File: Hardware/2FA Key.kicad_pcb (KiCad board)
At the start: 2 copper layers, 35.2 x 18.5 mm, 22 parts, among them J1 USB_A_PCB_Edge_receptacle, SW1 Push Button, U1 USBLC6-2SC6, U2 ATECC608B-SSHDA, U3 AP2112K‑3.3, U4 STM32L432KCU6

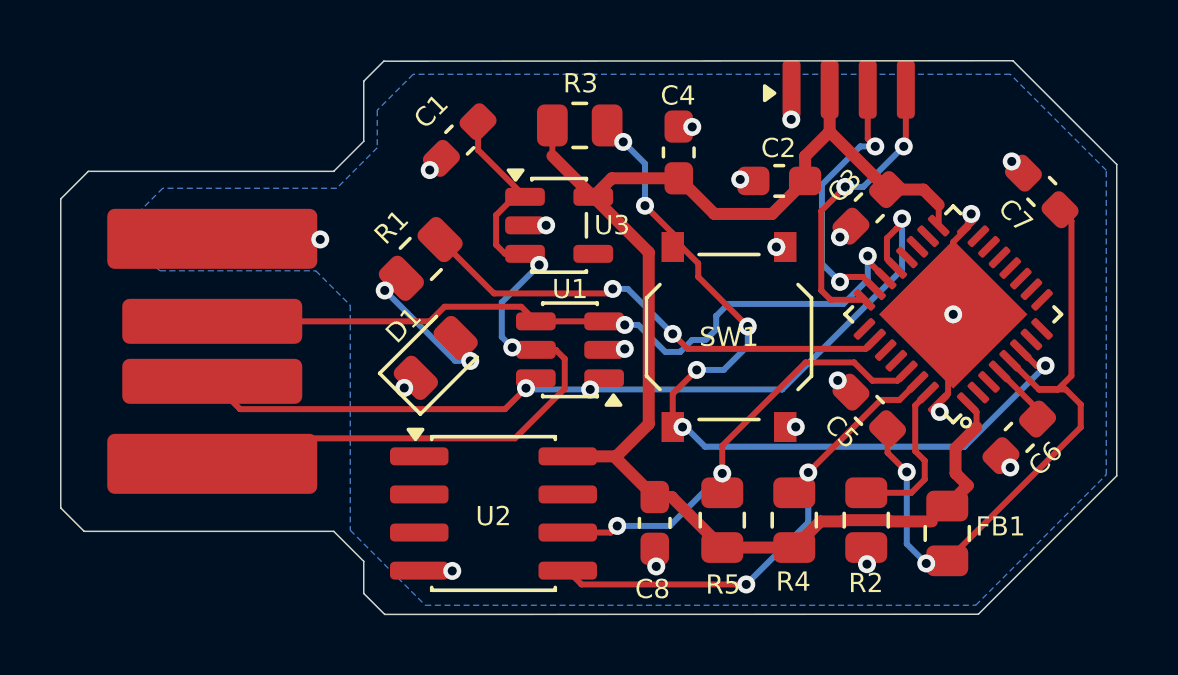
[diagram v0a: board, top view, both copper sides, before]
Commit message: Reorganize repo and rewrite README; add Ed25519 and compliance/programmable content
Move SSH guide to Guides/ and FIDO/RoHS docs to Compliance/; add Programmable/ (HID Injection, Mouse Jiggler, hardware, case), 3D Printable/, BOM datasheets, renders. Rewrite README around 2FAK V1C and Programmable 2FAK with Getting Started, Compliance, Resources, Credits. Resident firmware: Ed25519 (ed25519-sk) via TweetNaCl + provisioning docs. Ignore editor .history/.
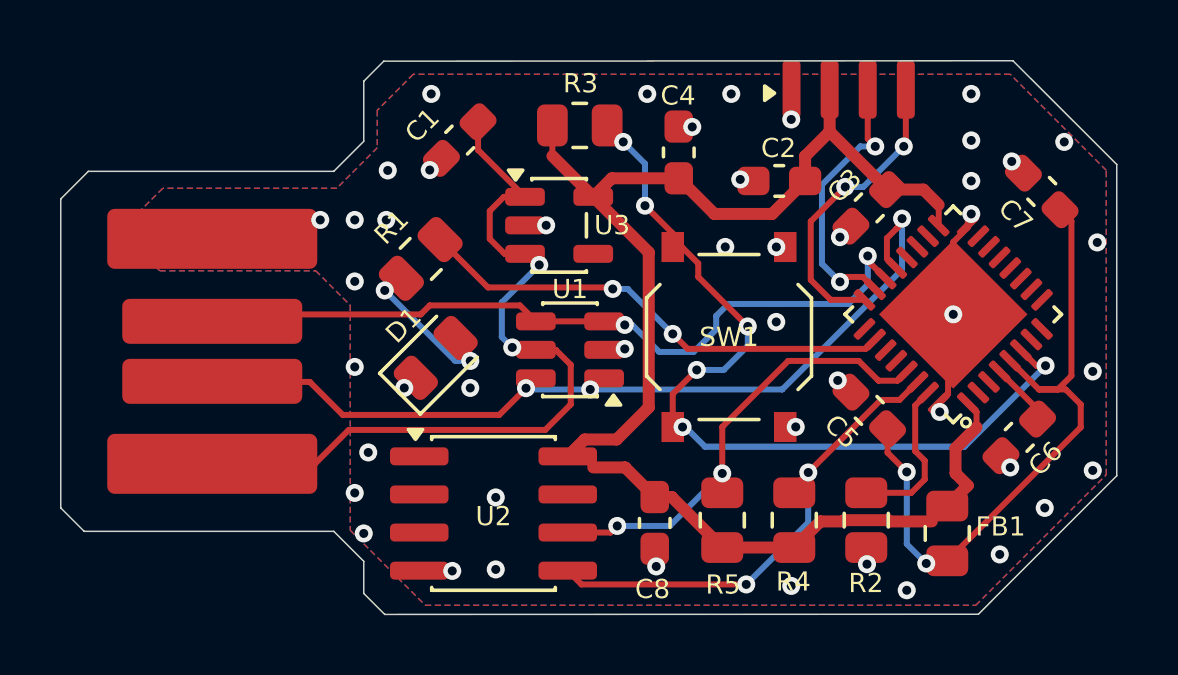
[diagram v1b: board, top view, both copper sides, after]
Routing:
- net GND: track 21.1 -> 17.5 mm, vias 20 -> 47
- net U1/1-C3: track 48.7 -> 50.2 mm
- net J1/1-U2/1-U2/3-U4/5-C1/1: track 26.2 -> 27.2 mm
- added copper zone on F.Cu, net GND

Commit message: Small update
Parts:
- C3: value 100nF -> 1uF
- C7: value 1uF -> 100nF
- R1: value 330 -> 10K
- R3: value 10K -> 4.7K
- R5: value 4.7K -> 330
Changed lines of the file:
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@@
 			(drillshape 0)
 			(scaleselection 1)
-			(outputdirectory "V1C Gerber/")
+			(outputdirectory "V1C/")
 		)
 	)
@@
 		(tags "capacitor handsolder")
 		(property "Reference" "C8"
-			(at 2.208839 0.073483 180)
+			(at 2.1 0.073483 180)
 			(layer "F.SilkS")
 			(effects
@@
 			)
 		)
-		(property "Value" "10K"
+		(property "Value" "4.7K"
 			(at 0 1.65 0)
 			(layer "F.Fab")
@@
 			)
 		)
-		(property "Value" "330"
+		(property "Value" "10K"
 			(at -2.5 0 45)
 			(layer "F.Fab")
@@
 			)
 		)
-		(property "Value" "4.7K"
+		(property "Value" "330"
 			(at 2.9125 -0.25 90)
 			(layer "F.Fab")
@@
 			)
 		)
-		(property "Value" "1uF"
+		(property "Value" "100nF"
 			(at 2.25 0 135)
 			(layer "F.Fab")
@@
 		(tags "capacitor handsolder")
 		(property "Reference" "C3"
-			(at 0.05972 1.104861 45)
+			(at 1.168236 1.094506 45)
 			(layer "F.SilkS")
 			(effects
@@
 			)
 		)
-		(property "Value" "100nF"
+		(property "Value" "1uF"
 			(at 3.25 -0.015626 45)
 			(layer "F.Fab")
@@
 	)
 	(segment
-		(start 150.5 105.387499)
-		(end 149.512501 104.4)
-		(width 0.4)
-		(layer "F.Cu")
-		(net "U1{slash}1-C3")
-	)
-	(segment
-		(start 148.45 104.4)
-		(end 148.16875 104.11875)
-		(width 0.2)
-		(layer "F.Cu")
-		(net "U1{slash}1-C3")
-	)
-	(segment
-		(start 147.68875 104.11875)
-		(end 147.6 104.03)
-		(width 0.2)
-		(layer "F.Cu")
-		(net "U1{slash}1-C3")
-	)
-	(segment
 		(start 156.02 106.2)
 		(end 155.15 107.07)
@@
 	)
 	(segment
-		(start 148.45 104.4)
-		(end 148.772501 104.4)
-		(width 0.2)
-		(layer "F.Cu")
-		(net "U1{slash}1-C3")
-	)
-	(segment
-		(start 148.16875 104.11875)
-		(end 147.68875 104.11875)
-		(width 0.2)
-		(layer "F.Cu")
-		(net "U1{slash}1-C3")
-	)
-	(segment
 		(start 159.965632 95.647954)
 		(end 159.455663 95.137985)
@@
 	)
 	(segment
-		(start 160.526517 103.758839)
-		(end 161.226517 103.058839)
+		(start 147.6 104.03)
+		(end 147.97 104.4)
 		(width 0.4)
 		(layer "F.Cu")
@@
 	)
 	(segment
-		(start 154.412501 95.95)
-		(end 152.4875 95.95)
+		(start 160.526517 103.758839)
+		(end 161.226517 103.058839)
 		(width 0.4)
 		(layer "F.Cu")
@@
 	)
 	(segment
-		(start 149.512501 104.4)
-		(end 148.45 104.4)
+		(start 154.412501 95.95)
+		(end 152.4875 95.95)
 		(width 0.4)
 		(layer "F.Cu")
@@
 	)
 	(segment
+		(start 149.512501 104.4)
+		(end 150.5 105.387499)
+		(width 0.4)
+		(layer "F.Cu")
+		(net "U1{slash}1-C3")
+	)
+	(segment
 		(start 160.25 105.6875)
 		(end 159.7375 106.2)
@@
 	)
 	(segment
+		(start 147.97 104.4)
+		(end 149.512501 104.4)
+		(width 0.4)
+		(layer "F.Cu")
+		(net "U1{slash}1-C3")
+	)
+	(segment
+		(start 147.97 104.4)
+		(end 148.772501 104.4)
+		(width 0.2)
+		(layer "F.Cu")
+		(net "U1{slash}1-C3")
+	)
+	(segment
 		(start 151.875 101.175)
 		(end 151.9 101.15)
@@
 		(layer "F.Cu")
 		(hatch none 0.1)
-		(priority 30026)
+		(priority 30000)
+		(attr
+			(teardrop
+				(type padvia)
+			)
+		)
+		(connect_pads yes
+			(clearance 0)
+		)
+		(min_thickness 0.0254)
+		(fill yes
+			(island_removal_mode 1)
+		)
+		(polygon
+			(pts
+				(xy 149.875074 104.47973) (xy 149.592231 104.762573) (xy 150.025 105.584251) (xy 150.500707 105.388206)
+				(xy 150.634252 104.849999)
+			)
+		)
+	)
+	(zone
+		(net "U1{slash}1-C3")
+		(layer "F.Cu")
+		(hatch none 0.1)
+		(priority 30001)
 		(attr
 			(teardrop
@@
 		(layer "F.Cu")
 		(hatch none 0.1)
-		(priority 30038)
+		(priority 30002)
 		(attr
 			(teardrop
@@
 		(layer "F.Cu")
 		(hatch none 0.1)
-		(priority 30000)
+		(priority 30016)
 		(attr
 			(teardrop
@@
 	)
 	(zone
-		(net "U1{slash}1-C3")
-		(layer "F.Cu")
-		(hatch none 0.1)
-		(priority 30027)
-		(attr
-			(teardrop
-				(type padvia)
-			)
-		)
-		(connect_pads yes
-			(clearance 0)
-		)
-		(min_thickness 0.0254)
-		(fill yes
-			(island_removal_mode 1)
-		)
-		(polygon
-			(pts
-				(xy 148.651005 104.6) (xy 148.651005 104.2) (xy 148.591421 104.258579) (xy 148.575 104.100736) (xy 147.839293 103.789293)
-				(xy 147.955736 104.33) (xy 148.308579 104.541421) (xy 148.45 104.6)
-			)
-		)
-	)
-	(zone
 		(net "U1{slash}PH3-R1")
 		(layer "F.Cu")
@@
 			)
 		)
-	)
-	(zone
-		(net "U1{slash}1-C3")
-		(layer "F.Cu")
-		(hatch none 0.1)
-		(priority 30008)
-		(attr
-			(teardrop
-				(type padvia)
-			)
-		)
-		(connect_pads yes
-			(clearance 0)
-		)
-		(min_thickness 0.0254)
-		(fill yes
-			(island_removal_mode 1)
-		)
-		(polygon
-			(pts
-				(xy 149.875074 104.47973) (xy 149.592231 104.762573) (xy 150.025 105.584251) (xy 150.500707 105.388206)
-				(xy 150.634252 104.849999)
-			)
-		)
